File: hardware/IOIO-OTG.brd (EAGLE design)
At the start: 68.6 x 30.5 mm, 60 parts, among them Q1 IRLML2244, Q2 2N7002PW, Q3 AO3404A, U1 PIC24FJ256GB206, U14 SWITCH_SPDT, U2 TPS62133RGTT, U3 VREG_MIC5216

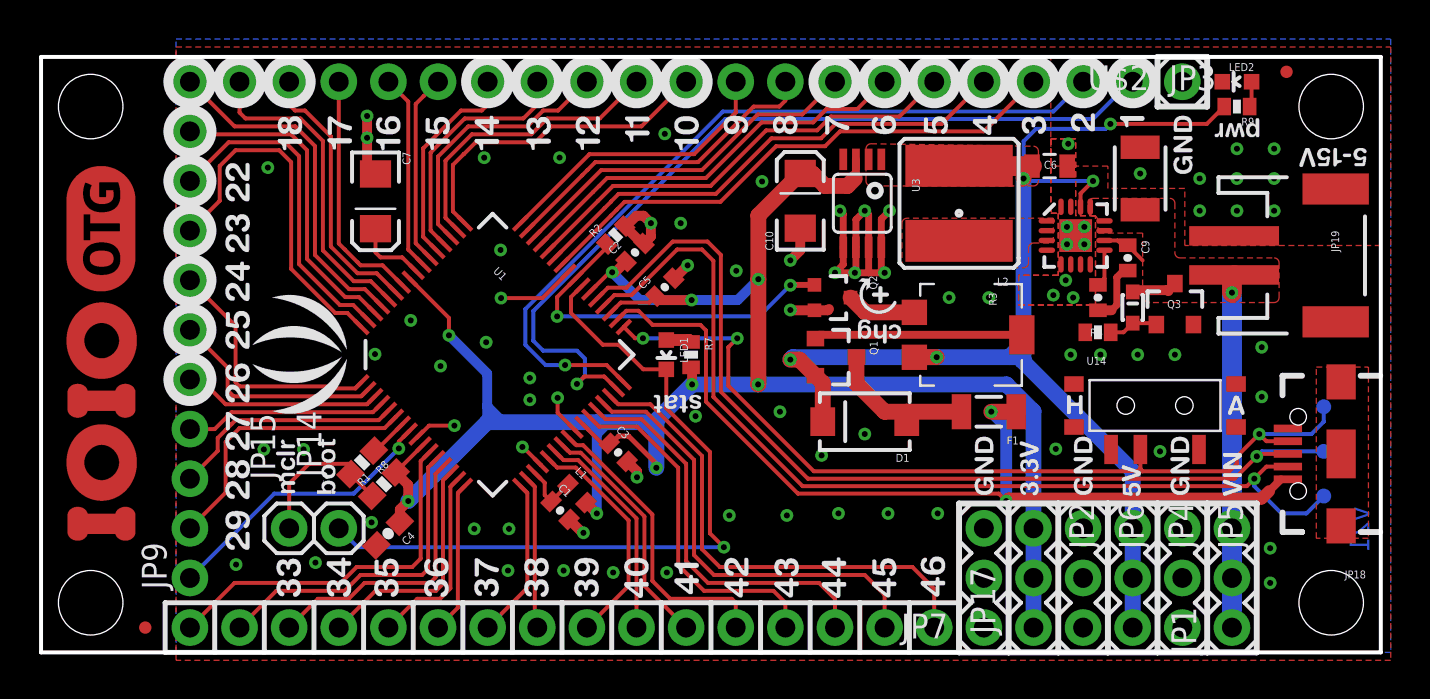
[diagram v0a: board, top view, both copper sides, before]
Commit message: Moved C1 and L1 to proper 0603 packages
moved X/Y coordinates
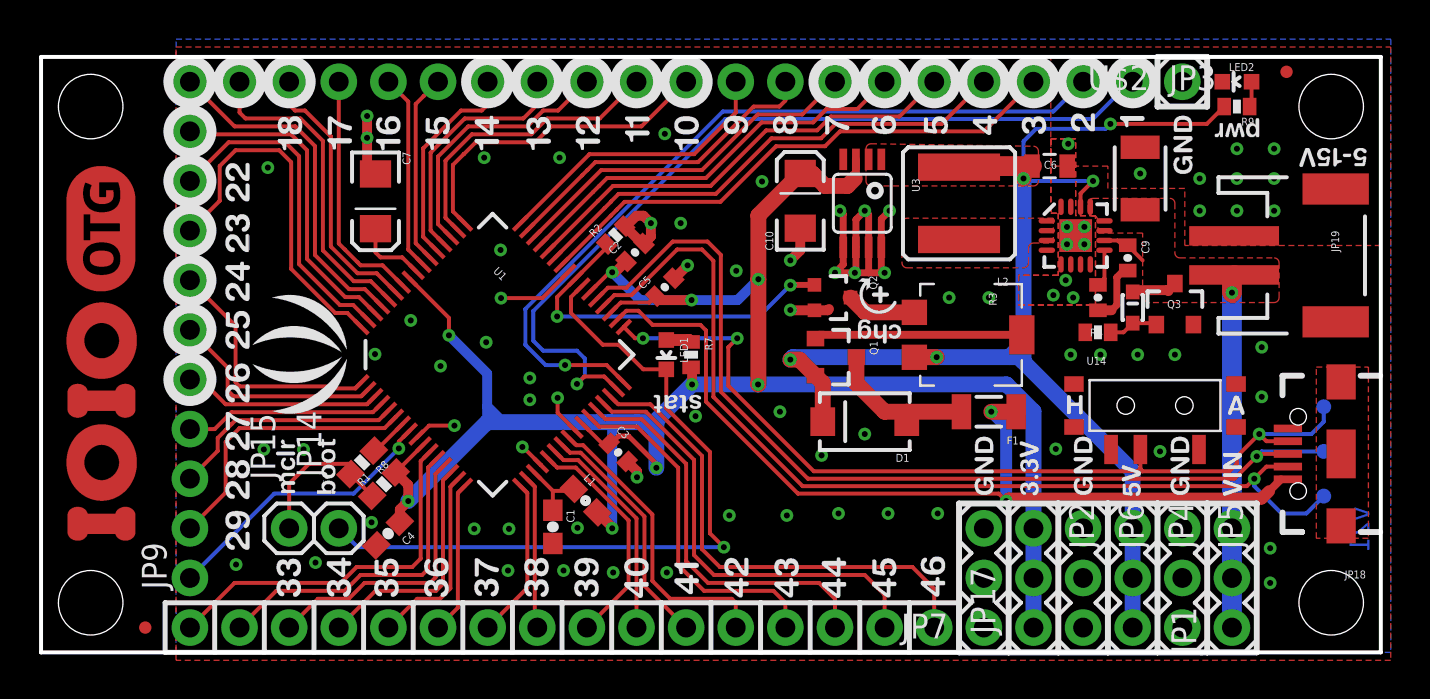
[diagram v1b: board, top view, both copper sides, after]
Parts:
- C1: device SparkFun:0402-CAP -> SparkFun-Capacitors:0603-CAP
- L1: device SparkFun-Passives:C0402 -> SparkFun-Passives:0603
- moved C1 0.92 mm to (26.2, 6.43), turned to 270 degrees
- moved L1 0.57 mm to (27.9, 7.77)
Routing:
- net 3.3V: track 111.0 -> 112.2 mm
- net GND: track 43.3 -> 42.3 mm
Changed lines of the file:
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@@
 <layer number="20" name="Dimension" color="15" fill="1" visible="yes" active="yes"/>
 <layer number="21" name="tPlace" color="16" fill="1" visible="yes" active="yes"/>
-<layer number="22" name="bPlace" color="14" fill="1" visible="yes" active="yes"/>
+<layer number="22" name="bPlace" color="14" fill="1" visible="no" active="yes"/>
 <layer number="23" name="tOrigins" color="15" fill="1" visible="yes" active="yes"/>
 <layer number="24" name="bOrigins" color="15" fill="1" visible="yes" active="yes"/>
@@
 <attribute name="VALUE" x="18.87135625" y="15.24" size="0.4064" layer="27" rot="R315"/>
 </element>
-<element name="C1" library="SparkFun" package="0402-CAP" value="0.1uF" x="26.5684" y="7.2644" smashed="yes" rot="R315">
-<attribute name="NAME" x="26.433696875" y="8.386934375" size="0.4064" layer="25" rot="R315"/>
-<attribute name="VALUE" x="24.99685625" y="7.2195" size="0.4064" layer="27" rot="R315"/>
+<element name="C1" library="SparkFun-Capacitors" package="0603-CAP" value="0.1uF" x="26.19791875" y="6.4262" smashed="yes" rot="R270">
+<attribute name="NAME" x="26.896421875" y="7.3152" size="0.4064" layer="25" rot="R270"/>
+<attribute name="VALUE" value="0.1uF" x="25.054921875" y="7.5057" size="0.4064" layer="27" rot="R270"/>
+<attribute name="PROD_ID" value="CAP-00810" x="26.19791875" y="6.4262" size="1.778" layer="27" rot="R270" display="off"/>
 </element>
 <element name="C2" library="SparkFun" package="0402-CAP" value="0.1uF" x="30.4038" y="20.4724" smashed="yes" rot="R45">
@@
 <attribute name="PART#" value="TS53YL502MR10" x="46.99" y="13.97" size="1.778" layer="21" rot="R90" display="off"/>
 </element>
-<element name="L1" library="SparkFun-Passives" package="C0402" value="30Ohm,1.8A" x="27.432" y="8.128" smashed="yes" rot="R315">
-<attribute name="NAME" x="27.29729375" y="9.25053125" size="0.4064" layer="25" rot="R315"/>
-<attribute name="VALUE" x="25.860453125" y="8.083096875" size="0.4064" layer="27" rot="R315"/>
+<element name="L1" library="SparkFun-Passives" package="0603" value="30Ohm,1.8A" x="27.872515625" y="7.768040625" smashed="yes" rot="R315">
+<attribute name="NAME" x="27.737809375" y="8.89056875" size="0.4064" layer="25" rot="R315"/>
+<attribute name="VALUE" x="26.30096875" y="7.7231375" size="0.4064" layer="27" rot="R315"/>
+<attribute name="PROD_ID" value="RES-07859" x="27.872515625" y="7.768040625" size="1.778" layer="27" rot="R315" display="off"/>
 </element>
 <element name="U14" library="SparkFun-Electromechanical" package="KPS-1290" value="SWITCH_SPDT" x="57.023" y="12.6365" smashed="yes" rot="R180">
@@
 <wire x1="28.829" y1="10.585659375" x2="28.829" y2="10.540996875" width="0.2032" layer="1"/>
 <wire x1="28.829" y1="10.540996875" x2="28.930596875" y2="10.540996875" width="0.2032" layer="1"/>
-<wire x1="27.89161875" y1="7.668378125" x2="27.891621875" y2="7.668378125" width="0.508" layer="1"/>
-<wire x1="27.891621875" y1="7.668378125" x2="28.448" y2="7.112" width="0.508" layer="1"/>
-<via x="28.448" y="7.112" extent="1-16" drill="0.3048" diameter="0.635"/>
+<via x="29.2354" y="6.35" extent="1-16" drill="0.3048" diameter="0.635"/>
 <via x="31.496" y="9.4488" extent="1-16" drill="0.3048" diameter="0.635"/>
 <wire x1="29.154359375" y1="10.7696" x2="29.080578125" y2="10.69581875" width="0.508" layer="1"/>
@@
 <wire x1="30.0736" y1="11.0744" x2="31.496" y2="9.652" width="0.254" layer="1"/>
 <wire x1="31.496" y1="9.4488" x2="31.496" y2="9.652" width="0.254" layer="1"/>
-<wire x1="28.448" y1="7.112" x2="28.448" y2="11.176" width="0.508" layer="16"/>
-<wire x1="28.448" y1="11.176" x2="28.448" y2="11.684" width="0.508" layer="16"/>
 <wire x1="28.448" y1="11.684" x2="28.5496" y2="11.7856" width="0.508" layer="16"/>
-<wire x1="28.5496" y1="11.7856" x2="31.3944" y2="11.7856" width="0.8128" layer="16"/>
+<wire x1="28.5496" y1="11.7856" x2="29.1338" y2="11.7856" width="0.8128" layer="16"/>
+<wire x1="29.1338" y1="11.7856" x2="30.5054" y2="11.7856" width="0.8128" layer="16"/>
+<wire x1="30.5054" y1="11.7856" x2="31.3944" y2="11.7856" width="0.8128" layer="16"/>
 <wire x1="31.3944" y1="11.7856" x2="33.3248" y2="13.716" width="0.8128" layer="16"/>
 <wire x1="31.496" y1="9.4488" x2="31.496" y2="11.176" width="0.8128" layer="16"/>
@@
 <wire x1="28.829" y1="10.585659375" x2="28.939159375" y2="10.69581875" width="0.2032" layer="1"/>
 <wire x1="28.939159375" y1="10.69581875" x2="29.080578125" y2="10.69581875" width="0.2032" layer="1"/>
-<wire x1="28.448" y1="11.176" x2="27.919534375" y2="11.704465625" width="0.508" layer="16"/>
 <wire x1="27.919534375" y1="11.704465625" x2="27.71019375" y2="11.704465625" width="0.508" layer="16"/>
-<wire x1="28.448" y1="11.176" x2="28.956" y2="11.684" width="0.508" layer="16"/>
 <wire x1="28.956" y1="11.684" x2="29.0576" y2="11.684" width="0.508" layer="16"/>
 <wire x1="31.3944" y1="11.176" x2="30.8864" y2="11.684" width="0.508" layer="16"/>
@@
 <wire x1="18.796" y1="7.747" x2="18.796" y2="8.56808125" width="0.508" layer="1"/>
 <wire x1="18.796" y1="8.56808125" x2="18.152440625" y2="9.211640625" width="0.508" layer="1"/>
+<wire x1="29.2354" y1="6.35" x2="29.2354" y2="11.7856" width="0.508" layer="16"/>
+<wire x1="29.2354" y1="11.7856" x2="30.5054" y2="11.7856" width="0.508" layer="16"/>
+<wire x1="29.0576" y1="11.684" x2="29.0576" y2="11.7856" width="0.508" layer="16"/>
+<wire x1="29.0576" y1="11.7856" x2="29.1338" y2="11.7856" width="0.508" layer="16"/>
+<wire x1="28.47355625" y1="7.166996875" x2="29.2354" y2="6.405153125" width="0.508" layer="1"/>
+<wire x1="29.2354" y1="6.405153125" x2="29.2354" y2="6.35" width="0.508" layer="1"/>
+<wire x1="27.71019375" y1="11.704465625" x2="27.71019375" y2="11.704465625" width="0" layer="19" extent="1-16"/>
 </signal>
 <signal name="GND">
@@
 <via x="26.7462" y="4.191" extent="1-16" drill="0.3048" diameter="0.635"/>
 <via x="29.2862" y="4.0894" extent="1-16" drill="0.3048" diameter="0.635"/>
-<via x="27.7622" y="6.1214" extent="1-16" drill="0.3048" diameter="0.635"/>
-<wire x1="27.7622" y1="6.1214" x2="27.711396875" y2="6.1214" width="0.508" layer="1"/>
-<wire x1="27.711396875" y1="6.1214" x2="27.02801875" y2="6.804778125" width="0.508" layer="1"/>
+<via x="27.4574" y="6.3754" extent="1-16" drill="0.3048" diameter="0.635"/>
 <via x="30.5054" y="8.9662" extent="1-16" drill="0.3048" diameter="0.635"/>
 <wire x1="30.5054" y1="8.9662" x2="30.5054" y2="9.270996875" width="0.508" layer="1"/>
@@
 <contactref element="C1" pad="1"/>
 <contactref element="U1" pad="19"/>
-<wire x1="25.781" y1="8.051796875" x2="25.781" y2="8.6839125" width="0.2032" layer="1"/>
-<wire x1="25.781" y1="8.6839125" x2="25.23531875" y2="9.229590625" width="0.2032" layer="1"/>
-<wire x1="25.781" y1="8.051796875" x2="26.108778125" y2="7.72401875" width="0.2032" layer="1"/>
-<wire x1="26.972378125" y1="8.58761875" x2="26.108778125" y2="7.72401875" width="0.2032" layer="1"/>
+<wire x1="25.23531875" y1="9.229590625" x2="26.19791875" y2="8.266990625" width="0.2032" layer="1"/>
+<wire x1="26.19791875" y1="8.266990625" x2="26.19791875" y2="7.2762" width="0.2032" layer="1"/>
+<wire x1="27.271471875" y1="8.36908125" x2="27.16938125" y2="8.266990625" width="0.2032" layer="1"/>
+<wire x1="27.16938125" y1="8.266990625" x2="26.19791875" y2="8.266990625" width="0.2032" layer="1"/>
 </signal>
 <signal name="BOOT">

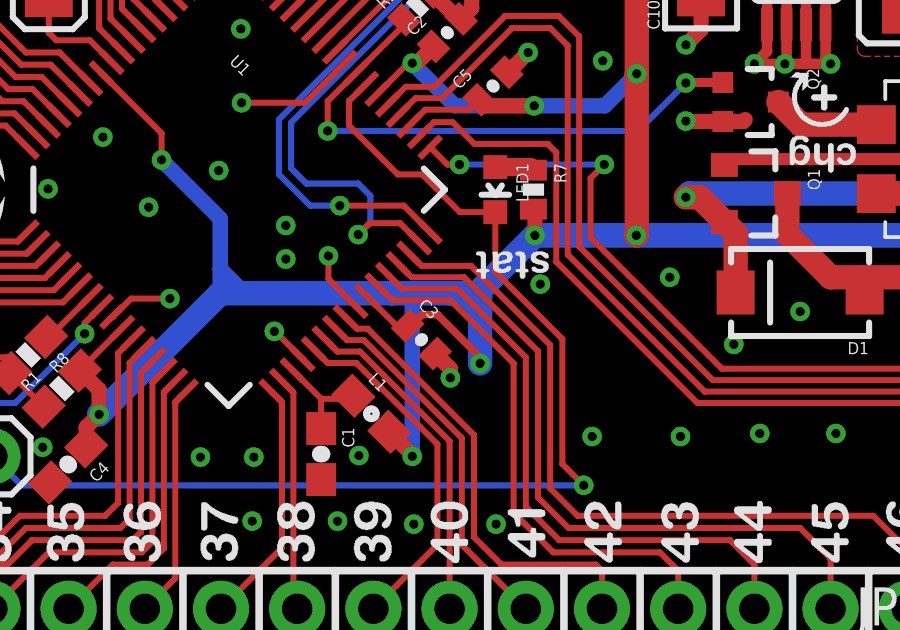
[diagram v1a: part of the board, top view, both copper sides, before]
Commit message: Moved C3 to proper 0603 package
moved X/Y coordinate
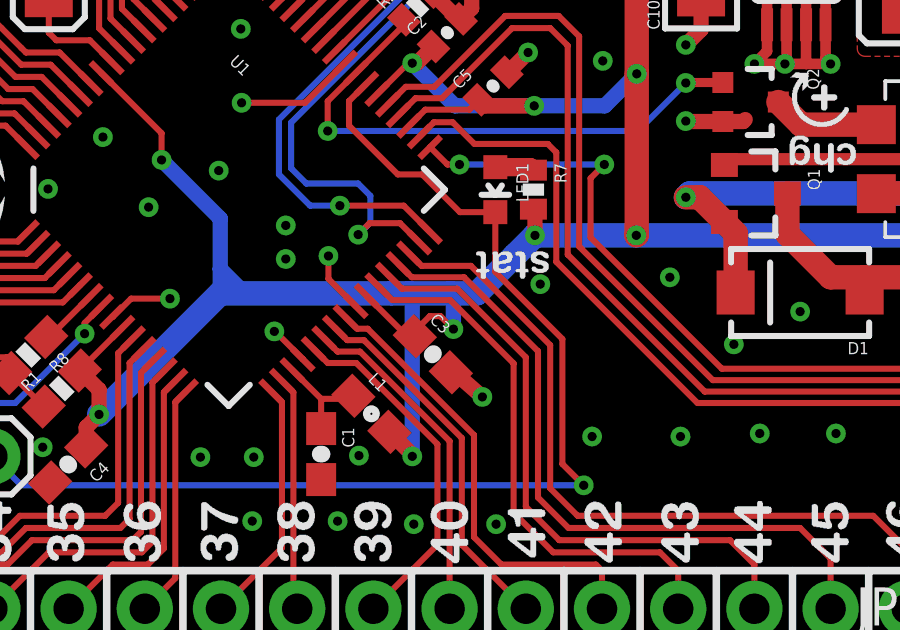
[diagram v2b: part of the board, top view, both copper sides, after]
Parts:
- C3: device SparkFun:0402-CAP -> SparkFun-Capacitors:0603-CAP
- moved C3 0.61 mm to (29.9, 9.75)
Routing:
- net 3.3V: track 112.2 -> 109.2 mm
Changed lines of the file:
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@@
 <attribute name="VALUE" x="30.4487" y="18.900853125" size="0.4064" layer="27" rot="R45"/>
 </element>
-<element name="C3" library="SparkFun" package="0402-CAP" value="0.1uF" x="29.5402" y="10.2362" smashed="yes" rot="R315">
-<attribute name="NAME" x="29.405496875" y="11.358734375" size="0.4064" layer="25" rot="R315"/>
-<attribute name="VALUE" x="27.96865625" y="10.1913" size="0.4064" layer="27" rot="R315"/>
+<element name="C3" library="SparkFun-Capacitors" package="0603-CAP" value="0.1uF" x="29.9212" y="9.7536" smashed="yes" rot="R315">
+<attribute name="NAME" x="29.786496875" y="10.876134375" size="0.4064" layer="25" rot="R315"/>
+<attribute name="VALUE" value="0.1uF" x="28.34965625" y="9.7087" size="0.4064" layer="27" rot="R315"/>
+<attribute name="PROD_ID" value="CAP-00810" x="29.9212" y="9.7536" size="1.778" layer="27" rot="R315" display="off"/>
 </element>
 <element name="C4" library="SparkFun-Capacitors" package="0603-CAP" value="0.1uF" x="17.7645875" y="6.080590625" smashed="yes" rot="R225">
@@
 <wire x1="36.718" y1="19.1008" x2="36.718" y2="13.731" width="0.8128" layer="1"/>
 <wire x1="36.718" y1="13.731" x2="36.703" y2="13.716" width="0.8128" layer="1"/>
-<wire x1="28.829" y1="10.585659375" x2="28.829" y2="10.540996875" width="0.2032" layer="1"/>
-<wire x1="28.829" y1="10.540996875" x2="28.930596875" y2="10.540996875" width="0.2032" layer="1"/>
 <via x="29.2354" y="6.35" extent="1-16" drill="0.3048" diameter="0.635"/>
-<via x="31.496" y="9.4488" extent="1-16" drill="0.3048" diameter="0.635"/>
-<wire x1="29.154359375" y1="10.7696" x2="29.080578125" y2="10.69581875" width="0.508" layer="1"/>
+<via x="30.607" y="10.5918" extent="1-16" drill="0.3048" diameter="0.635"/>
 <wire x1="36.703" y1="13.716" x2="36.6014" y2="13.8176" width="0.508" layer="16" curve="90"/>
 <wire x1="36.703" y1="13.716" x2="33.3248" y2="13.716" width="0.8128" layer="16"/>
@@
 <wire x1="33.2994" y1="18.034" x2="31.66895625" y2="18.034" width="0.508" layer="1"/>
 <wire x1="31.66895625" y1="18.034" x2="31.468178125" y2="18.234778125" width="0.508" layer="1"/>
-<wire x1="29.080578125" y1="10.69581875" x2="29.18701875" y2="10.69581875" width="0.254" layer="1"/>
-<wire x1="29.18701875" y1="10.69581875" x2="29.5656" y2="11.0744" width="0.254" layer="1"/>
-<wire x1="29.5656" y1="11.0744" x2="30.0736" y2="11.0744" width="0.254" layer="1"/>
-<wire x1="30.0736" y1="11.0744" x2="31.496" y2="9.652" width="0.254" layer="1"/>
-<wire x1="31.496" y1="9.4488" x2="31.496" y2="9.652" width="0.254" layer="1"/>
 <wire x1="28.448" y1="11.684" x2="28.5496" y2="11.7856" width="0.508" layer="16"/>
 <wire x1="28.5496" y1="11.7856" x2="29.1338" y2="11.7856" width="0.8128" layer="16"/>
 <wire x1="29.1338" y1="11.7856" x2="30.5054" y2="11.7856" width="0.8128" layer="16"/>
 <wire x1="30.5054" y1="11.7856" x2="31.3944" y2="11.7856" width="0.8128" layer="16"/>
-<wire x1="31.3944" y1="11.7856" x2="33.3248" y2="13.716" width="0.8128" layer="16"/>
-<wire x1="31.496" y1="9.4488" x2="31.496" y2="11.176" width="0.8128" layer="16"/>
-<wire x1="31.496" y1="11.684" x2="31.3944" y2="11.7856" width="0.8128" layer="16"/>
-<wire x1="27.71019375" y1="11.704465625" x2="28.718840625" y2="10.69581875" width="0.2032" layer="1"/>
-<wire x1="28.718840625" y1="10.69581875" x2="29.080578125" y2="10.69581875" width="0.2032" layer="1"/>
-<wire x1="28.829" y1="10.585659375" x2="28.939159375" y2="10.69581875" width="0.2032" layer="1"/>
-<wire x1="28.939159375" y1="10.69581875" x2="29.080578125" y2="10.69581875" width="0.2032" layer="1"/>
-<wire x1="27.919534375" y1="11.704465625" x2="27.71019375" y2="11.704465625" width="0.508" layer="16"/>
+<wire x1="31.3944" y1="11.7856" x2="32.6644" y2="13.0556" width="0.8128" layer="16"/>
+<wire x1="32.6644" y1="13.0556" x2="33.3248" y2="13.716" width="0.8128" layer="16"/>
 <wire x1="28.956" y1="11.684" x2="29.0576" y2="11.684" width="0.508" layer="16"/>
-<wire x1="31.3944" y1="11.176" x2="30.8864" y2="11.684" width="0.508" layer="16"/>
-<wire x1="31.496" y1="11.176" x2="31.496" y2="11.684" width="0.8128" layer="16"/>
-<wire x1="31.496" y1="11.176" x2="30.988" y2="11.684" width="0.254" layer="16"/>
 <wire x1="30.988" y1="11.684" x2="30.8864" y2="11.684" width="0.254" layer="16"/>
 <wire x1="18.87135625" y1="19.129084375" x2="18.87135625" y2="19.12704375" width="0.2032" layer="1"/>
@@
 <wire x1="28.47355625" y1="7.166996875" x2="29.2354" y2="6.405153125" width="0.508" layer="1"/>
 <wire x1="29.2354" y1="6.405153125" x2="29.2354" y2="6.35" width="0.508" layer="1"/>
-<wire x1="27.71019375" y1="11.704465625" x2="27.71019375" y2="11.704465625" width="0" layer="19" extent="1-16"/>
+<wire x1="31.9024" y1="12.2936" x2="32.6644" y2="13.0556" width="0.508" layer="16"/>
+<wire x1="30.8864" y1="11.684" x2="30.7848" y2="11.7856" width="0.254" layer="16"/>
+<wire x1="30.7848" y1="11.7856" x2="30.5054" y2="11.7856" width="0.254" layer="16"/>
+<wire x1="30.607" y1="10.5918" x2="30.607" y2="11.684" width="0.508" layer="16"/>
+<wire x1="30.607" y1="11.684" x2="30.5054" y2="11.7856" width="0.508" layer="16"/>
+<wire x1="29.32015625" y1="10.354640625" x2="29.32015625" y2="10.52415625" width="0.2032" layer="1"/>
+<wire x1="29.32015625" y1="10.52415625" x2="29.8196" y2="11.0236" width="0.2032" layer="1"/>
+<wire x1="29.8196" y1="11.0236" x2="30.1752" y2="11.0236" width="0.2032" layer="1"/>
+<wire x1="30.1752" y1="11.0236" x2="30.607" y2="10.5918" width="0.2032" layer="1"/>
+<wire x1="27.71019375" y1="11.704465625" x2="29.06001875" y2="10.354640625" width="0.2032" layer="1"/>
+<wire x1="29.06001875" y1="10.354640625" x2="29.32015625" y2="10.354640625" width="0.2032" layer="1"/>
 </signal>
 <signal name="GND">
@@
 <via x="62.484" y="13.081" extent="1-16" drill="0.3048" diameter="0.635"/>
 <contactref element="U14" pad="S"/>
-<wire x1="27.356640625" y1="11.3509125" x2="27.356640625" y2="11.378359375" width="0.2032" layer="1"/>
 <via x="57.277" y="10.287" extent="1-16" drill="0.3048" diameter="0.635"/>
 <via x="23.5458" y="18.1356" extent="1-16" drill="0.3048" diameter="0.635"/>
@@
 <via x="29.2862" y="4.0894" extent="1-16" drill="0.3048" diameter="0.635"/>
 <via x="27.4574" y="6.3754" extent="1-16" drill="0.3048" diameter="0.635"/>
-<via x="30.5054" y="8.9662" extent="1-16" drill="0.3048" diameter="0.635"/>
-<wire x1="30.5054" y1="8.9662" x2="30.5054" y2="9.270996875" width="0.508" layer="1"/>
-<wire x1="30.5054" y1="9.270996875" x2="29.99981875" y2="9.776578125" width="0.508" layer="1"/>
+<via x="31.5722" y="8.3312" extent="1-16" drill="0.3048" diameter="0.635"/>
+<wire x1="31.5722" y1="8.3312" x2="30.5054" y2="9.270996875" width="0.508" layer="1"/>
+<wire x1="30.5054" y1="9.270996875" x2="30.522240625" y2="9.15255625" width="0.508" layer="1"/>
 <wire x1="39.588" y1="17.511" x2="38.369" y2="17.511" width="0.508" layer="1"/>
 <wire x1="38.369" y1="17.511" x2="38.354" y2="17.526" width="0.508" layer="1"/>
